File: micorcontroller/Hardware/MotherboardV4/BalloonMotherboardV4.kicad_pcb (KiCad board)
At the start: 4 copper layers, 85.9 x 82 mm, 248 parts, among them IC1 ITS4200S-ME-O, IC10 ITS4200S-ME-O, IC11 ITS4200S-ME-O, IC12 LM2596SX-5.0_NOPB, IC2 W5500, IC3 MCP1826S-5002E_DB, IC4 ITS4200S-ME-O, IC5 MS561101BA03-50, IC6 ITS4200S-ME-O, IC7 ITS4200S-ME-O, IC8 ITS4200S-ME-O, IC9 ITS4200S-ME-O, J1 693072010801, J3 J1B1211CCD, J4 GSB1C41110SSHR, Q1 FDN304P, U1 TLV9002QDRQ1, U3 LM2904AVQDRQ1, Y1 ECS-250-6-33B2-CTP-TR, Y2 ABM8G-12.000MHZ-4Y-T3

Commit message: some moving around
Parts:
- removed IC12: LM2596SX-5.0_NOPB, SamacSys_Parts:KTT0005B
- removed R20: 49.9, Resistor_SMD:R_0603_1608Metric_Pad0.98x0.95mm_HandSolder
- C39: value 0.1u -> 22u; footprint Capacitor_SMD:C_0402_1005Metric_Pad0.74x0.62mm_HandSolder -> Capacitor_SMD:C_0805_2012Metric_Pad1.18x1.45mm_HandSolder
- C66: value DNP -> 12p
- R19: value 0 -> DNP
- R24: value 10.2k -> 10k
- R47: value 53.6k -> 64.9k
- moved C25 1.27 mm to (64.3, 110.5)
- moved C38 1.27 mm to (66.8, 110.5)
- moved C39 1.27 mm to (68.8, 110.5)
- moved L1 1.27 mm to (65.5, 103.1)
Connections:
- C66 pad 1: Net-(C66-Pad1) -> /Power/5VBuck
- R47 pad 2: Net-(C66-Pad1) -> /Power/5VBuck
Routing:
- net Net-(C66-Pad1): track 11.8 -> 0.00 mm
- net /Power/5VBuck: track 75.2 -> 86.6 mm
- net unconnected-(IC12-OUTPUT-Pad2): vias 1 -> 0
- net GND: vias 252 -> 253

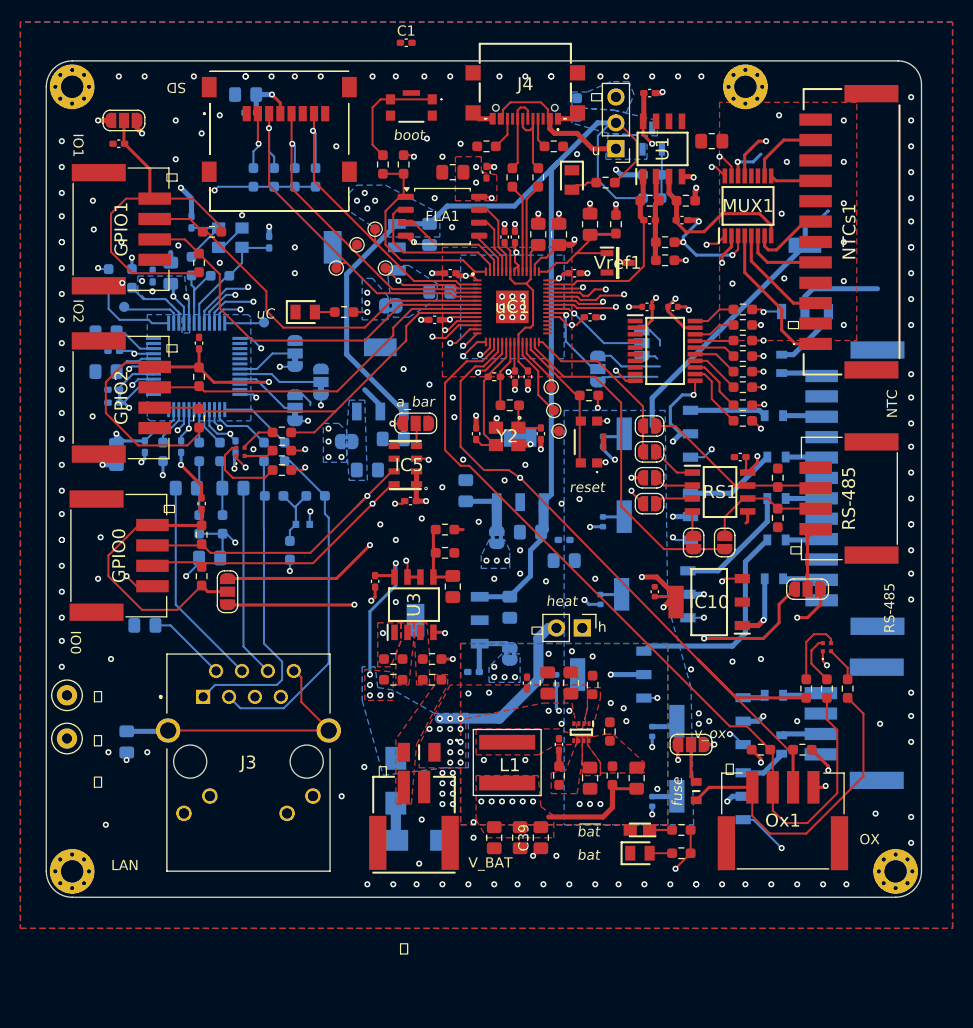
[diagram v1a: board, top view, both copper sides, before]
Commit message: added NTC calculation
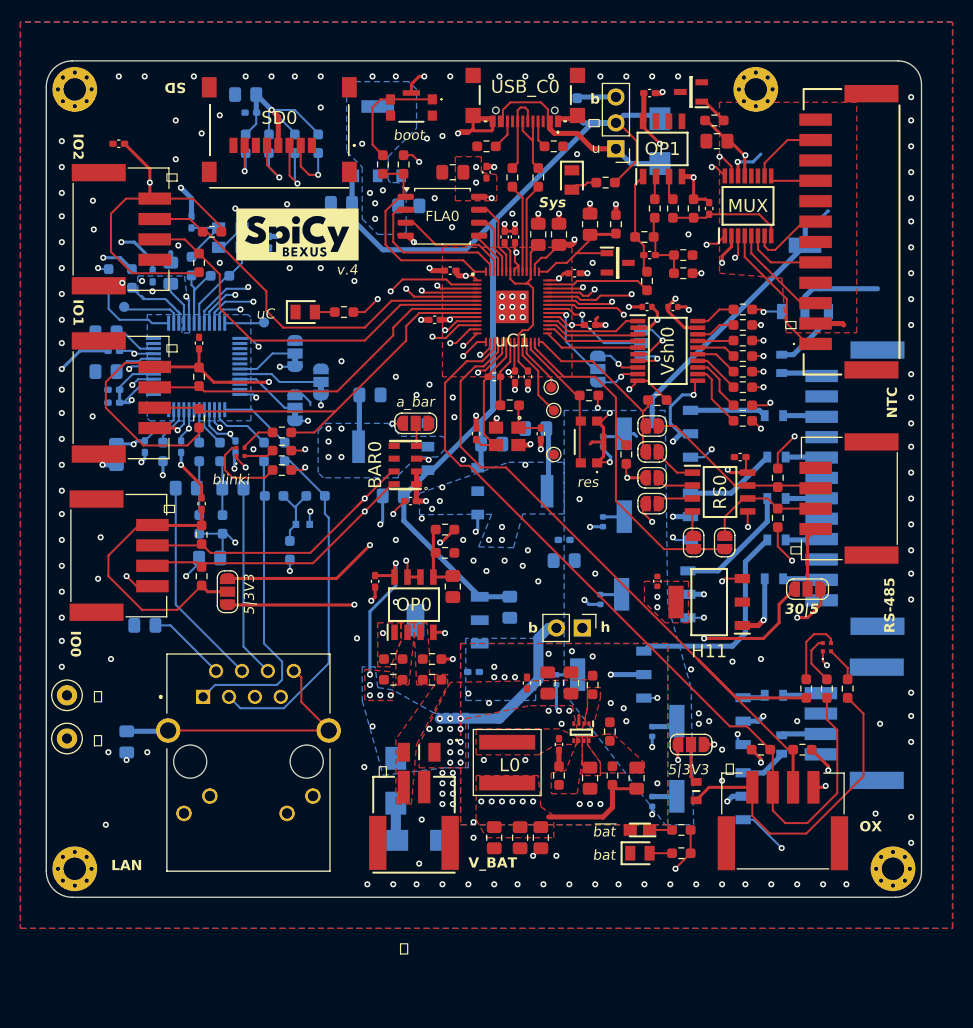
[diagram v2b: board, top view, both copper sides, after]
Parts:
- removed 3VLIN1, 3VLIN2, 3VLIN3: LM3940IMP-3.3_NOPB, SamacSys_Parts:SOT230P700X180-4N
- removed the C1 at (55.6, 32.5)
- removed the C3 at (54.4, 71.4)
- removed the C7 at (61.5, 76.5)
- removed C76: 0.1u, Capacitor_SMD:C_0402_1005Metric_Pad0.74x0.62mm_HandSolder
- removed C77: 2u2, Capacitor_SMD:C_0805_2012Metric_Pad1.18x1.45mm_HandSolder
- removed the J1 at (43.2, 42.2)
- removed JP14: SolderJumper_3_Open, Jumper:SolderJumper-3_P1.3mm_Open_RoundedPad1.0x1.5mm_NumberLabels
- removed the JP2 at (49.8, 71.6)
- removed the JP3 at (54.1, 58.3)
- removed the JP4 at (65.8, 92.5)
- removed the JP5 at (64.5, 81.0)
- removed Q1: FDN304P, SamacSys_Parts:SOT95P237X112-3N
- removed the R78 at (79.8, 47.8)
- removed the R80 at (72.4, 38.9)
- removed R81, R82: 10k, Resistor_SMD:R_0603_1608Metric_Pad0.98x0.95mm_HandSolder
- removed the R83 at (44.7, 45.7)
- removed the R84 at (46.7, 45.7)
- removed the TP2 at (52.6, 50.8)
- removed the TP3 at (50.8, 52.3)
- removed the TP4 at (48.8, 54.6)
- removed TP5: TestPoint, TestPoint:TestPoint_Pad_D1.0mm
- removed V_shifter1: TXS0108EQPWRQ1, SamacSys_Parts:SOP65P640X120-20N
- added C0: 10u, Capacitor_SMD:C_0805_2012Metric_Pad1.18x1.45mm_HandSolder, B.Cu at (64.0, 71.9)
- added C2: 10u, Capacitor_SMD:C_0805_2012Metric_Pad1.18x1.45mm_HandSolder, B.Cu at (54.4, 77.0)
- added C59: 2u2, Capacitor_SMD:C_0805_2012Metric_Pad1.18x1.45mm_HandSolder, B.Cu at (39.9, 37.6)
- added C60: 0.1u, Capacitor_SMD:C_0402_1005Metric_Pad0.74x0.62mm_HandSolder, B.Cu at (40.4, 39.4)
- added D0: RBR2LB60BTBR1, SamacSys_Parts:DIOM5336X245N, B.Cu at (80.5, 42.2)
- added G***: LOGO, SamacSys_Parts:Logo, F.Cu at (45.0, 51.3)
- added LRlan0: NCP1117ST33T3G, SamacSys_Parts:SOT230P700X180-4N, B.Cu at (54.4, 72.1)
- added LRre0: NCP1117ST33T3G, SamacSys_Parts:SOT230P700X180-4N, B.Cu at (66.0, 76.5)
- added LRuC0: NCP1117ST33T3G, SamacSys_Parts:SOT230P700X180-4N, B.Cu at (52.8, 42.2)
- added R36: 270, Resistor_SMD:R_0603_1608Metric_Pad0.98x0.95mm_HandSolder, F.Cu at (85.9, 40.1)
- added R43: 1k, Resistor_SMD:R_0603_1608Metric_Pad0.98x0.95mm_HandSolder, F.Cu at (80.0, 48.8)
- added R44: 1k, Resistor_SMD:R_0603_1608Metric_Pad0.98x0.95mm_HandSolder, F.Cu at (81.8, 48.8)
- added R47: 1k, Resistor_SMD:R_0603_1608Metric_Pad0.98x0.95mm_HandSolder, F.Cu at (79.2, 55.9)
- added R63: 10k, Resistor_SMD:R_0603_1608Metric_Pad0.98x0.95mm_HandSolder, B.Cu at (39.9, 42.4)
- added R64: 10k, Resistor_SMD:R_0603_1608Metric_Pad0.98x0.95mm_HandSolder, B.Cu at (42.2, 42.4)
- added R65: 10k, Resistor_SMD:R_0603_1608Metric_Pad0.98x0.95mm_HandSolder, B.Cu at (44.7, 42.4)
- added R66: 10k, Resistor_SMD:R_0603_1608Metric_Pad0.98x0.95mm_HandSolder, B.Cu at (47.0, 42.4)
- added R85: 100, Resistor_SMD:R_0603_1608Metric_Pad0.98x0.95mm_HandSolder, F.Cu at (77.2, 72.9)
- added R86: 100, Resistor_SMD:R_0603_1608Metric_Pad0.98x0.95mm_HandSolder, F.Cu at (80.3, 67.6)
- added SD0: 693072010801, SamacSys_Parts:693072010801, F.Cu at (43.2, 39.9)
- added Vref1: LM4040BIM3-3.0_NOPB, SamacSys_Parts:SOT95P237X112-3N, F.Cu at (83.6, 37.3)
- added Vshi0: TXS0108EQPWRQ1, SamacSys_Parts:SOP65P640X120-20N, F.Cu at (81.3, 62.7)
- C1: renamed from C2; value 0.47uF -> 10u
- C4: value 0.47u -> 10u
- C5: value 33u -> 10u
- C6: value 33uF -> 10u
- R2: renamed from R79; value 100k -> 0
- R37: renamed from R36; value missing -> 5k
- R38: renamed from R45; value missing -> 10k
- R39: renamed from R44; value missing -> 72,5k
- R45: renamed from R46; value missing -> 10k
- moved C5 26.2 mm to (55.9, 48.5)
- moved C6 12.3 mm to (52.1, 67.1)
- moved C4 10.2 mm to (68.3, 70.4)
- moved R2 9.89 mm to (72.4, 38.9), turned to 90 degrees
- moved C1 9.16 mm to (49.3, 48.3), turned to 0 degrees
- moved R45 3.59 mm to (79.0, 51.6)
- moved C39 3.43 mm to (79.5, 53.3)
- moved C38 2.90 mm to (85.3, 48.8), turned to -90 degrees
- moved TP2 2.34 mm to (70.1, 72.9)
- moved R38 2.18 mm to (82.8, 53.3)
- moved R39 2.18 mm to (82.8, 55.1)
- moved R37 1.08 mm to (83.8, 48.8), turned to 90 degrees
- moved C68 1.05 mm to (80.3, 85.3)
- moved H1 1.05 mm to (89.9, 37.1)
- moved C30 0.76 mm to (73.7, 60.2)
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- renumbered !bat1 to !bat0, 5sys1 to 5sys0, IC5 to BAR0, BUCK1 to BUCK0, C22 to C10, C66 to C11, C67 to C12, C25 to C13, C11 to C14, C14 to C15, C38 to C16, C39 to C18, C61 to C19, C69 to C20, C57 to C21, C21 to C22, C44 to C23, C46 to C24, C47 to C25, C40 to C26, C37 to C27, C36 to C28, C19 to C29, C62 to C3, C18 to C30, C13 to C31, C48 to C32, C51 to C33, C50 to C34, C49 to C35, C63 to C36, C60 to C37, C64 to C38, C65 to C39, C20 to C40, C68 to C41, C26 to C42, C15 to C43, C16 to C44, C27 to C45, C28 to C46, C29 to C47, C30 to C48, C31 to C49, C32 to C50, C33 to C51, C34 to C52, C45 to C53, C35 to C54, C42 to C55, C43 to C56, C52 to C57, C9 to C58, C53 to C61, C10 to C62, C56 to C63, C58 to C64, C59 to C65, C75 to C66, C55 to C67, C70 to C68, C12 to C69, C8 to C7, C71 to C70, C72 to C71, C24 to C72, C54 to C8, C23 to C9, D3 to D1, D1 to D2, F4 to F0, F9 to F3, F3 to F4, FB1 to FB0, FLA1 to FLA0, GPIO1 to GPIO0, GPIO2 to GPIO1, GPIO0 to GPIO2, H1 to H0, H2 to H1, H1-1 to H1-0, IC9 to H10, IC10 to H11, H3 to H2, H4 to H3, H3-1 to H3-0, IC1 to H4, IC4 to H5, IC11 to H6, IC6 to H7, IC7 to H8, IC8 to H9, J3 to J1, JB_or_U1 to JB_or_U0, JH1 to JH0, JH2 to JH1, JH3 to JH2, JHEAT1 to JHEAT0, JP13 to JP0, JP7 to JP1, JP15 to JP2, JP8 to JP3, JP9 to JP4, JP10 to JP5, JP1 to JP6, JP6 to JP7, JP11 to JP8, JP12 to JP9, JPVOX2 to JPVOX0, L1 to L0, IC2 to LAN1, LED1 to LED0, LED2 to LED1, IC3 to LR5V0, MUX1 to MUX, NTCs1 to NTCs0, U3 to OP0, U1 to OP1, Ox1 to Ox0, R21 to R0, R22 to R1, R52 to R10, R19 to R11, R53 to R12, R54 to R13, R48 to R14, R47 to R15, R24 to R16, R62 to R17, R64 to R18, R59 to R19, R63 to R20, R65 to R21, R58 to R22, R34 to R23, R35 to R24, R12 to R25, R41 to R26, R25 to R27, R60 to R28, R1 to R29, R2 to R30, R3 to R31, R61 to R32, R42 to R33, R43 to R34, R26 to R35, R5 to R40, R55 to R41, R56 to R42, R10 to R46, R9 to R48, R8 to R49, R17 to R5, R7 to R50, R15 to R51, R16 to R52, R27 to R53, R29 to R54, R30 to R55, R31 to R56, R32 to R57, R33 to R58, R37 to R59, R28 to R6, R38 to R60, R13 to R61, R14 to R62, R39 to R67, R40 to R68, R49 to R7, R4 to R72, R57 to R73, R77 to R74, R67 to R78, R69 to R79, R50 to R8, R71 to R80, R73 to R83, R75 to R84, R51 to R9, RS-485 to RS-0, RS1 to RS0, R_shunt1 to R_shunt0, S_BOOT1 to S_BOOT0, S_RES1 to S_RES0, TP12 to TP0, TP18 to TP1, TP1 to TP2, TP15 to TP3, TP16 to TP4, TPGND1 to TPGND0, TPGND2 to TPGND1, J4 to USB_C0, V_BAT1 to V_BAT0, Vref1 to Vref0, Y2 to Y0, bat1 to bat0, uC2 to uC0
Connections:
- net /Ethernet/F- renamed /EthernetaSD/F-
- net /Ethernet/LED_LAN_A renamed /EthernetaSD/LED_LAN_A
- net /Ethernet/LED_LAN_B renamed /EthernetaSD/LED_LAN_B
- net /Ethernet/RCT renamed /EthernetaSD/RCT
- net /Ethernet/RXN renamed /EthernetaSD/RXN
- net /Ethernet/RXP renamed /EthernetaSD/RXP
- net /Ethernet/TCT renamed /EthernetaSD/TCT
- net /Ethernet/TXN renamed /EthernetaSD/TXN
- net /Ethernet/TXP renamed /EthernetaSD/TXP
- net /Ethernet/XI renamed /EthernetaSD/XI
- net /Ethernet/Xo renamed /EthernetaSD/Xo
- net /Ethernet/cs_lan renamed /EthernetaSD/cs_lan
- net /Ethernet/miso_lan renamed /EthernetaSD/miso_lan
- net /Ethernet/mosi_lan renamed /EthernetaSD/mosi_lan
- net /Ethernet/sck_lan renamed /EthernetaSD/sck_lan
- C1 pad 2: /Power/5VSys -> /Power/VSys
- C11 pad 1: /Power/5VBuck -> /Power/VBuck
- C13 pad 2: /Power/5VBuck -> /Power/VBuck
- C16 pad 2: /Power/5VBuck -> /Power/VBuck
- C18 pad 2: /Power/5VBuck -> /Power/VBuck
- C19 pad 1: /Prozessor/GPIO1V -> /3V3_rest
- C3 pad 1: GND -> /Power/VSys
- C3 pad 2: /Power/5VSys -> GND
- C39 pad 1: /Prozessor/vol_Temp -> Net-(C39-Pad1)
- C39 pad 2: Net-(U1A--) -> /Sensors/op-
- C4 pad 2: /Power/5VSys -> /3V3_rest
- C41 pad 2: /5V -> /3V3_rest
- C43 pad 2: /Ethernet/3V3 -> /3V3lan
- C44 pad 2: /Ethernet/3V3 -> /3V3lan
- C47 pad 2: /Ethernet/3V3 -> /3V3lan
- C48 pad 2: /Ethernet/3V3 -> /3V3lan
- C49 pad 2: /Ethernet/3V3 -> /3V3lan
- C5 pad 2: Net-(3VLIN1-OUT) -> /Power/3V3_uC
- C50 pad 2: /Ethernet/3V3 -> /3V3lan
- C51 pad 2: /Ethernet/3V3 -> /3V3lan
- C52 pad 2: /Ethernet/3V3 -> /3V3lan
- C53 pad 2: /Ethernet/3V3 -> /3V3lan
- C6 pad 2: Net-(3VLIN3-OUT) -> /3V3lan
- C7 pad 2: Net-(IC3-VOUT) -> /5V
- FB0 pad 2: /Ethernet/3V3 -> /3V3lan
- GPIO0 pad 4: /Prozessor/GPIO1V -> /3V3_rest
- J1 pad 10: /Ethernet/3V3 -> /3V3lan
- J1 pad 12: /Ethernet/3V3 -> /3V3lan
- JB_or_U0 pad 2: /Power/5VSys -> /Power/VSys
- JB_or_U0 pad 3: /Power/5VBuck -> /Power/VBuck
- JH0 pad 1: /Ethernet/3V3 -> /3V3lan
- JH1 pad 1: /Ethernet/3V3 -> /3V3lan
- JH2 pad 1: /Ethernet/3V3 -> /3V3lan
- JP1 pad 1: /Prozessor/H2 -> /Heater/H3
- JP1 pad 3: /Prozessor/H3 -> /Heater/H2
- JP2 pad 1: /Prozessor/H0 -> /Heater/H1
- JP2 pad 3: /Prozessor/H1 -> /Heater/H0
- JP3 pad 1: /Prozessor/sclrs -> /Sensors/B
- JP3 pad 2: /Sensors/B -> /Prozessor/sclrs
- L0 pad 2: /Power/5VBuck -> /Power/VBuck
- LAN1 pad 11: /Ethernet/3V3 -> /3V3lan
- LAN1 pad 15: /Ethernet/3V3 -> /3V3lan
- LAN1 pad 17: /Ethernet/3V3 -> /3V3lan
- LAN1 pad 21: /Ethernet/3V3 -> /3V3lan
- LAN1 pad 28: /Ethernet/3V3 -> /3V3lan
- LAN1 pad 37: /Ethernet/3V3 -> /3V3lan
- LAN1 pad 4: /Ethernet/3V3 -> /3V3lan
- LAN1 pad 8: /Ethernet/3V3 -> /3V3lan
- LED0 pad 1: /Ethernet/3V3 -> /3V3lan
- LR5V0 pad 1: /Power/5VSys -> /Power/VSys
- LR5V0 pad 3: Net-(IC3-VOUT) -> /5V
- NTCs0 pad 10: /3V3_rest -> /Sensors/ntc+
- NTCs0 pad 12: /3V3_rest -> /Sensors/ntc+
- NTCs0 pad 2: /3V3_rest -> /Sensors/ntc+
- NTCs0 pad 4: /3V3_rest -> /Sensors/ntc+
- NTCs0 pad 6: /3V3_rest -> /Sensors/ntc+
- NTCs0 pad 8: /3V3_rest -> /Sensors/ntc+
- OP1 pad 1: /Prozessor/vol_Temp -> Net-(C39-Pad1)
- OP1 pad 2: Net-(U1A--) -> Net-(OP1A--)
- OP1 pad 3: /Sensors/ntc - -> Net-(OP1A-+)
- OP1 pad 8: /5V -> /3V3_rest
- R15 pad 2: /Power/5VBuck -> /Power/VBuck
- R17 pad 2: /Prozessor/GPIO1V -> /3V3_rest
- R2 pad 1: Net-(Q1-G) -> /Power/VSys
- R2 pad 2: GND -> /Power/VBuck
- R20 pad 2: /Prozessor/GPIO1V -> /3V3_rest
- R38 pad 2: Net-(U1A--) -> /Sensors/op-
- R39 pad 2: Net-(U1A--) -> /Sensors/op-
- R45 pad 1: /Prozessor/vol_Temp -> Net-(C39-Pad1)
- R45 pad 2: Net-(U1A--) -> /Sensors/op-
- R6 pad 2: /Power/5VSys -> /Power/VSys
- uC1 pad 2: /Prozessor/miso_sd -> /EthernetaSD/miso_sd
- uC1 pad 29: /Prozessor/H4 -> /Heater/H4
- uC1 pad 3: /Prozessor/cs_sd -> /EthernetaSD/cs_sd
- uC1 pad 30: /Prozessor/H5 -> /Heater/H5
- uC1 pad 31: /Prozessor/H6 -> /Heater/H6
- uC1 pad 32: /Prozessor/H7 -> /Heater/H7
- uC1 pad 4: /Prozessor/sck_sd -> /EthernetaSD/sck_sd
- uC1 pad 5: /Prozessor/mosi_sd -> /EthernetaSD/mosi_sd
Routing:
- net /3V3lan: track 0.00 -> 145.5 mm, vias 0 -> 18
- net /Ethernet/3V3: track 131.5 -> 0.00 mm, vias 21 -> 0
- net /Power/VSys: track 0.00 -> 127.3 mm
- net /Power/5VSys: track 118.0 -> 0.00 mm, vias 4 -> 0
- net /Power/VBuck: track 0.00 -> 90.0 mm, vias 0 -> 6
- net /Power/5VBuck: track 86.6 -> 0.00 mm, vias 6 -> 0
- net /3V3_rest: track 149.8 -> 196.4 mm, vias 28 -> 21
- net /Prozessor/mosi_sd: track 37.3 -> 0.00 mm, vias 1 -> 0
- net /Prozessor/GPIO1V: track 35.2 -> 0.00 mm
- net /Prozessor/cs_sd: track 34.7 -> 0.00 mm, vias 2 -> 0
- net /Prozessor/sck_sd: track 33.1 -> 0.00 mm, vias 1 -> 0
- net /Prozessor/miso_sd: track 32.8 -> 0.00 mm, vias 1 -> 0
- net /EthernetaSD/miso_sd: track 0.00 -> 32.7 mm, vias 0 -> 2
- net /EthernetaSD/sck_sd: track 0.00 -> 30.6 mm, vias 0 -> 2
- net /EthernetaSD/mosi_sd: track 0.00 -> 29.5 mm, vias 0 -> 2
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- added copper zone on In1.Cu, net /3V3_rest
- added copper zone on B.Cu, net /3V3lan
- added copper zone on In1.Cu, net /3V3lan
- added copper zone on F.Cu, net /Heater/Vs_Heat
- added copper zone on F.Cu, net /Power/VBuck
- added copper zone on In1.Cu, net /Power/VBuck
- added copper zone on F.Cu, net /Sensors/ntc+
- removed copper zone on F.Cu, net /3V3_rest
- removed copper zone on B.Cu, net /Ethernet/3V3
- removed copper zone on In1.Cu, net /Ethernet/3V3
- removed copper zone on B.Cu, net /Power/5VBuck
- removed copper zone on F.Cu, net /Power/5VBuck
- removed copper zone on In1.Cu, net /Power/5VBuck
- removed copper zone on B.Cu, net /Power/5VSys
- removed copper zone on B.Cu, net /Power/V_usb
- removed copper zone on B.Cu, net Net-(3VLIN1-OUT)
- removed copper zone on B.Cu, net Net-(3VLIN3-OUT)
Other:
- board text added: "30|5"
- board text added: "5|3V3"
- board text added: "H0|H1"
- board text added: "H2|H3"
- board text added: "Sys"
- board text added: "b"
- board text added: "blinki"
- board text added: "res"
- board text added: "v.4"
- board text removed: "fuse"
- board text removed: "heat"
- board text removed: "reset"
- board text removed: "v_ox"
